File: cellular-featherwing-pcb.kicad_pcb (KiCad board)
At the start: 2 copper layers, 27 x 54 mm, 9 parts, among them J1 SIM8060-6-0-14-00-A, J2 TSM-116-01-L-SV, J3 TSM-112-01-L-SV, U1 BG96, U2 TPS63020DSJR, U3 TXB0108DQSR, U4 MAX8868EUK30+, U5 SN74AHC1G09DCKR

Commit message: Routing progress
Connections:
- U3 pad 12: unconnected-(U3-Pad12) -> GSM_RI
- U5 pad 1: unconnected-(U5-Pad1) -> GSM_RI

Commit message: Add ufl connector
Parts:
- added J4: U.FL-R-SMT(10), U_fl_conn:HRS_U.FL-R-SMT(10), F.Cu at (175.3, 116.8)
- added J5: U.FL-R-SMT(10), U_fl_conn:HRS_U.FL-R-SMT(10), F.Cu at (170.0, 116.8)
- renumbered U5 to DD1
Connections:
- DD1 pad 2: unconnected-(U5-Pad2) -> GSM_RI
- DD1 pad 3: unconnected-(U5-Pad3) -> GND
- DD1 pad 4: unconnected-(U5-Pad4) -> Q_INT
- DD1 pad 5: unconnected-(U5-Pad5) -> 3V3

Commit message: schematic updates
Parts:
- moved J3 1.46 mm to (158.9, 93.0)
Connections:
- net Net-(U1-Pad32) renamed VBAT_BB
- net Net-(U1-Pad52) renamed VBAT_RF
- J2 pad 02: unconnected-(J2-Pad02) -> VDD
- J2 pad 04: unconnected-(J2-Pad04) -> GND
- J2 pad 05: unconnected-(J2-Pad05) -> GMS_STATUS_EXT
- J2 pad 09: unconnected-(J2-Pad09) -> Q_INT_EXT
- J2 pad 10: unconnected-(J2-Pad10) -> GSM_DCD_EXT
- J2 pad 14: unconnected-(J2-Pad14) -> GSM_TXD_ESP32
- J2 pad 15: unconnected-(J2-Pad15) -> GSM_RXD_ESP32
- J3 pad 01: unconnected-(J3-Pad01) -> VBAT
- J3 pad 03: unconnected-(J3-Pad03) -> 5V
- J3 pad 04: unconnected-(J3-Pad04) -> ENABLE
- J3 pad 05: unconnected-(J3-Pad05) -> GSM_RI_EXT
- J3 pad 06: unconnected-(J3-Pad06) -> GSM_TXD_ESP_RTS
- J3 pad 07: unconnected-(J3-Pad07) -> GSM_RXD_ESP_CTS
- J3 pad 09: unconnected-(J3-Pad09) -> MODEM_ON
- J3 pad 10: unconnected-(J3-Pad10) -> GSM_DTR_EXT
- J3 pad 11: unconnected-(J3-Pad11) -> I2C_SCL
- J3 pad 12: unconnected-(J3-Pad12) -> I2C_SDA
- U1 pad 10: unconnected-(U1-Pad10) -> USB_DN_GSM
- U1 pad 15: unconnected-(U1-Pad15) -> ON_PIN
- U1 pad 20: unconnected-(U1-Pad20) -> GSM_STATUS_INT
- U1 pad 21: unconnected-(U1-Pad21) -> GSM_NET
- U1 pad 22: unconnected-(U1-Pad22) -> DBG_RXD
- U1 pad 23: unconnected-(U1-Pad23) -> DBG_TXD
- U1 pad 27: unconnected-(U1-Pad27) -> GPS_TXD
- U1 pad 28: unconnected-(U1-Pad28) -> GPS_RXD
- U1 pad 29: unconnected-(U1-Pad29) -> VDD_EXT
- U1 pad 30: unconnected-(U1-Pad30) -> DTR
- U1 pad 34: unconnected-(U1-Pad34) -> RXD
- U1 pad 35: unconnected-(U1-Pad35) -> TXD
- U1 pad 36: unconnected-(U1-Pad36) -> CTS
- U1 pad 37: unconnected-(U1-Pad37) -> RTS
- U1 pad 38: unconnected-(U1-Pad38) -> DCD
- U1 pad 39: unconnected-(U1-Pad39) -> RI
- U1 pad 42: unconnected-(U1-Pad42) -> GND
- U1 pad 43: unconnected-(U1-Pad43) -> SIM_VDD
- U1 pad 44: unconnected-(U1-Pad44) -> SIM_RST
- U1 pad 45: unconnected-(U1-Pad45) -> SIM_DATA
- U1 pad 46: unconnected-(U1-Pad46) -> SIM_CLK
- U1 pad 47: unconnected-(U1-Pad47) -> GND
- U1 pad 49: unconnected-(U1-Pad49) -> GPS_ANT
- U1 pad 60: unconnected-(U1-Pad60) -> GSM_ANT
- U1 pad 75: unconnected-(U1-Pad75) -> USB_BOOT
- U1 pad 8: unconnected-(U1-Pad8) -> USB_VBUS_GSM
- U1 pad 9: unconnected-(U1-Pad9) -> USB_DP_GSM
- U3 pad 1: unconnected-(U3-Pad1) -> RXD
- U3 pad 10: unconnected-(U3-Pad10) -> GSM_STATUS_INT
- U3 pad 11: unconnected-(U3-Pad11) -> GSM_STATUS
- U3 pad 13: unconnected-(U3-Pad13) -> GSM_DCD
- U3 pad 14: unconnected-(U3-Pad14) -> GSM_DTR
- U3 pad 15: unconnected-(U3-Pad15) -> GND
- U3 pad 16: unconnected-(U3-Pad16) -> 3V3
- U3 pad 17: unconnected-(U3-Pad17) -> GSM_CTS
- U3 pad 18: unconnected-(U3-Pad18) -> GSM_RTS
- U3 pad 19: unconnected-(U3-Pad19) -> GSM_TXD
- U3 pad 2: unconnected-(U3-Pad2) -> TXD
- U3 pad 20: unconnected-(U3-Pad20) -> GSM_RXD
- U3 pad 3: unconnected-(U3-Pad3) -> RTS_GPS_RXD
- U3 pad 4: unconnected-(U3-Pad4) -> CTS_GPS_TXD
- U3 pad 5: unconnected-(U3-Pad5) -> VDD_EXT
- U3 pad 6: unconnected-(U3-Pad6) -> VDD_EXT
- U3 pad 7: unconnected-(U3-Pad7) -> DTR
- U3 pad 8: unconnected-(U3-Pad8) -> DCD
- U3 pad 9: unconnected-(U3-Pad9) -> RI

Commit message: More progress
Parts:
- added VT3: DTC043TEBTL, ul_DTC043TEBTL:DTC043TEBTL, F.Cu at (146.6, 132.7)
- added VT4: DTC043TEBTL, ul_DTC043TEBTL:DTC043TEBTL, F.Cu at (156.5, 132.7)

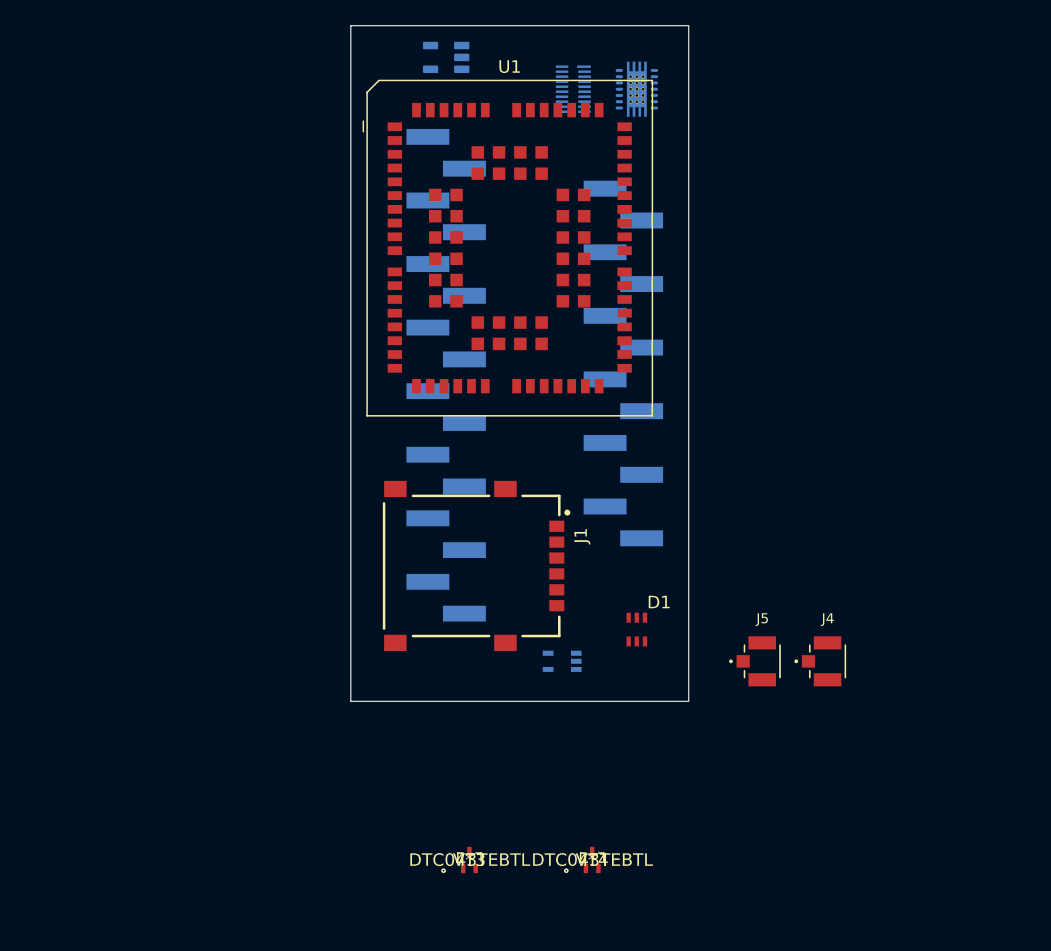
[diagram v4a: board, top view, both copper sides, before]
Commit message: Wired network LED in schematic
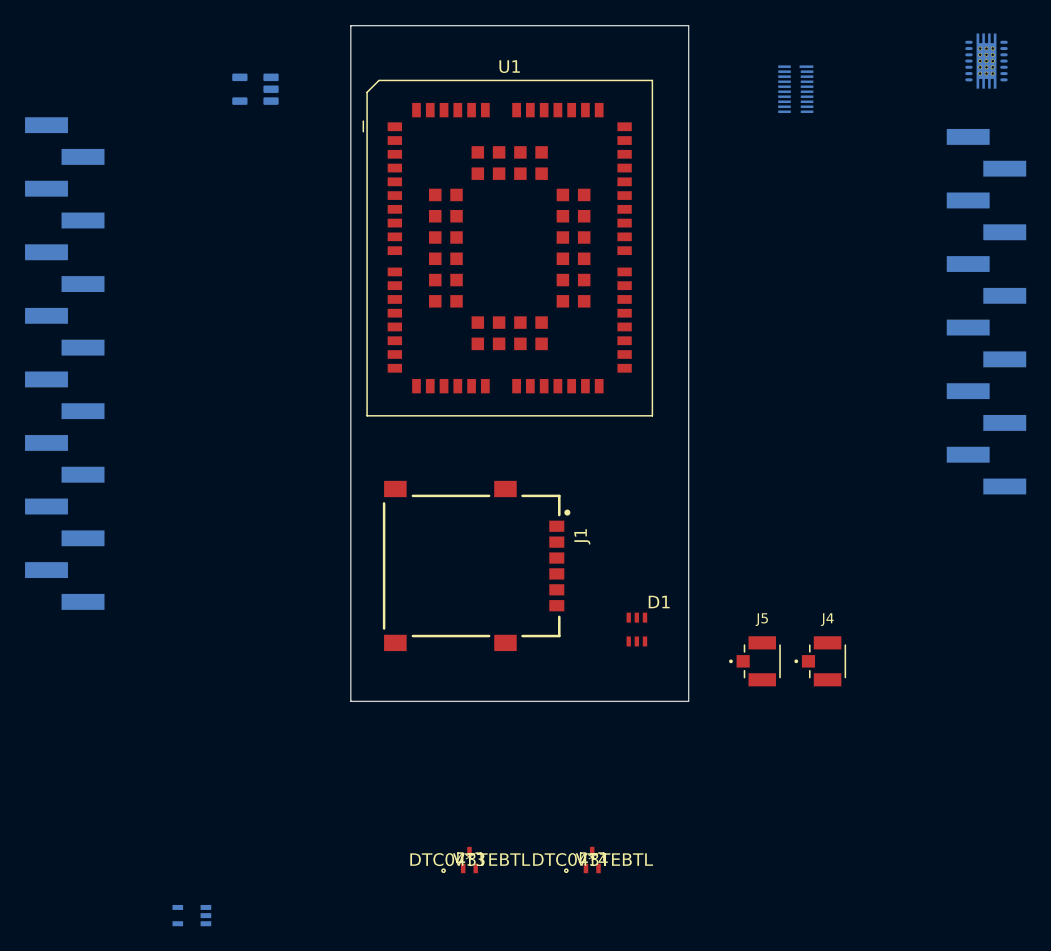
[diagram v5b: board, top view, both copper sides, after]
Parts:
- moved DD1 35.9 mm to (124.5, 137.2)
- moved J2 30.5 mm to (114.3, 93.0)
- moved J3 29.3 mm to (188.0, 88.9)
- moved U2 28.0 mm to (188.0, 68.9)
- moved U3 17.8 mm to (172.7, 71.1)
- moved U4 15.5 mm to (129.5, 71.1)
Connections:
- D1 pad 2: unconnected-(D1-Pad2) -> GND
- D1 pad 3: unconnected-(D1-Pad3) -> SIM_VDD
- D1 pad 4: unconnected-(D1-Pad4) -> Net-(J1-PadC2)
- D1 pad 6: unconnected-(D1-Pad6) -> Net-(J1-PadC3)
- J1 pad C1: unconnected-(J1-PadC1) -> SIM_VDD
- J1 pad C2: unconnected-(J1-PadC2) -> Net-(J1-PadC2)
- J1 pad C3: unconnected-(J1-PadC3) -> Net-(J1-PadC3)
- J1 pad C5: unconnected-(J1-PadC5) -> GND
- J1 pad C7: unconnected-(J1-PadC7) -> Net-(J1-PadC7)
- J1 pad S1: Net-(J1-PadS1) -> GND
- J1 pad S2: Net-(J1-PadS1) -> GND
- J1 pad S3: Net-(J1-PadS1) -> GND
- J1 pad S4: Net-(J1-PadS1) -> GND

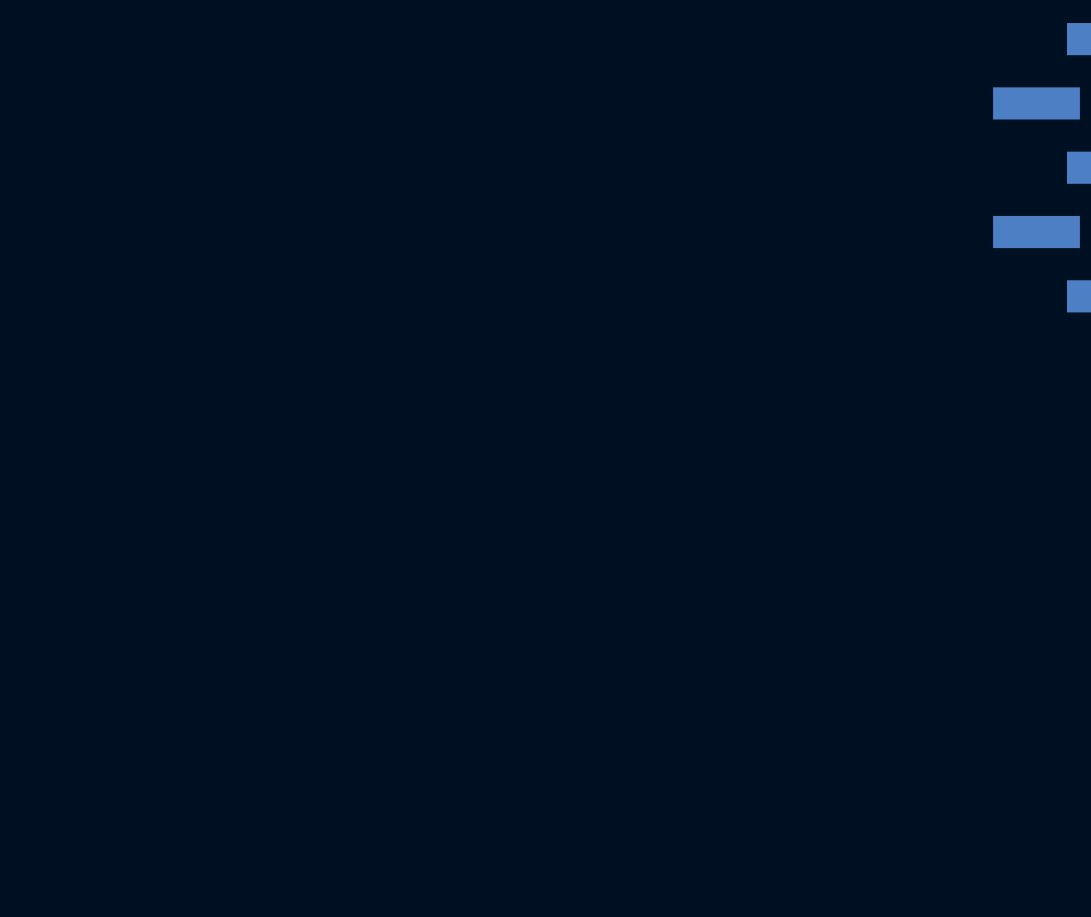
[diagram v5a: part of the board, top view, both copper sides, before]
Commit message: Wired all the jumpers
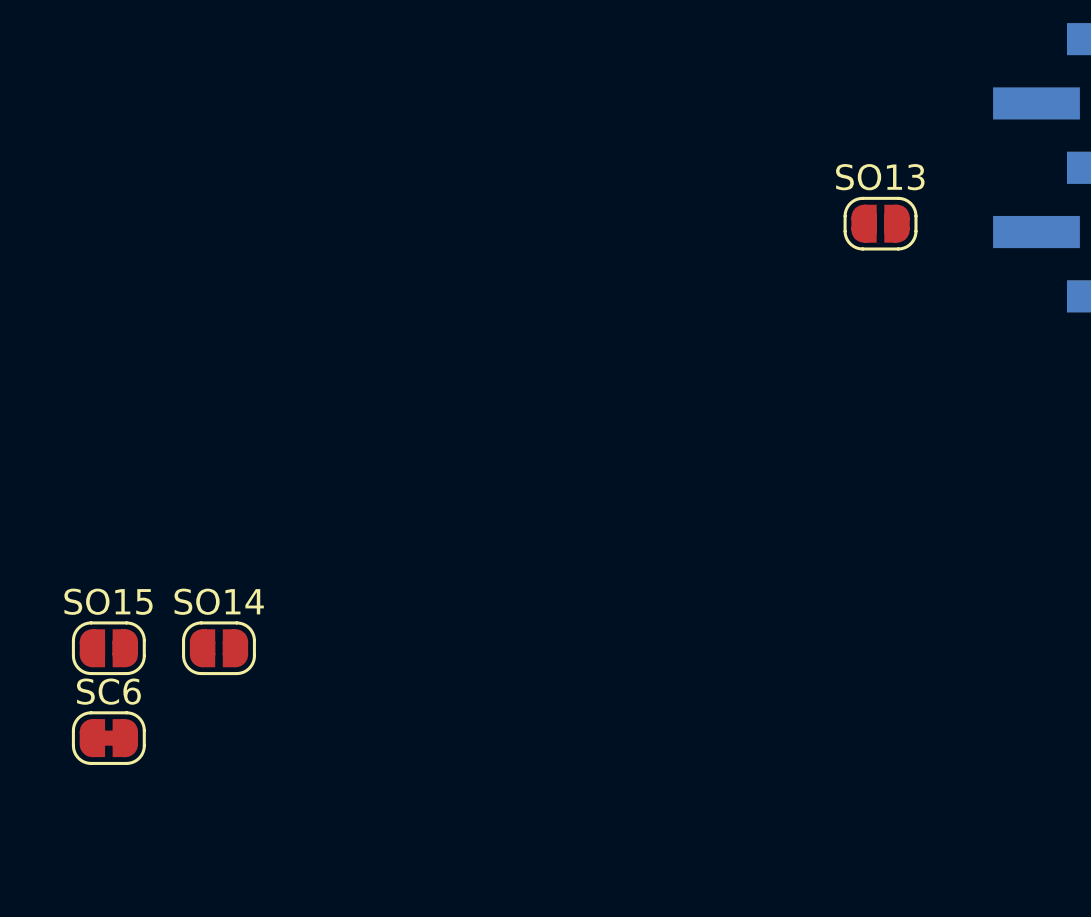
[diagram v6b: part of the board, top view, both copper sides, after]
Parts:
- added SC6: SolderJumper_2_Bridged, Jumper:SolderJumper-2_P1.3mm_Bridged_RoundedPad1.0x1.5mm, F.Cu at (76.2, 129.5)
- added SO13: SolderJumper_2_Open, Jumper:SolderJumper-2_P1.3mm_Open_RoundedPad1.0x1.5mm, F.Cu at (106.7, 109.2)
- added SO14: SolderJumper_2_Open, Jumper:SolderJumper-2_P1.3mm_Open_RoundedPad1.0x1.5mm, F.Cu at (80.5, 126.0)
- added SO15: SolderJumper_2_Open, Jumper:SolderJumper-2_P1.3mm_Open_RoundedPad1.0x1.5mm, F.Cu at (76.2, 126.0)
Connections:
- U4 pad 2: unconnected-(U4-Pad2) -> GND

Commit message: schematic complete
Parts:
- added C1: 22uF, Capacitor_SMD:C_0603_1608Metric, F.Cu at (177.8, 134.6)
- added C2: 22uF, Capacitor_SMD:C_0603_1608Metric, F.Cu at (177.8, 132.1)
- added C30: 4.7uF, Capacitor_SMD:C_0402_1005Metric, F.Cu at (73.7, 86.4)
- added C31: 4.7uF, Capacitor_SMD:C_0402_1005Metric, F.Cu at (68.1, 95.5)
- added C33: 4.7uF, Capacitor_SMD:C_0402_1005Metric, F.Cu at (71.0, 95.7)
- added C6: 22uF, Capacitor_SMD:C_0603_1608Metric, F.Cu at (181.8, 134.6)
- added C7: 22uF, Capacitor_SMD:C_0603_1608Metric, F.Cu at (177.8, 137.1)
- added C8: 22uF, Capacitor_SMD:C_0603_1608Metric, F.Cu at (181.8, 132.1)
- added L1: 1 uH, Inductor_SMD:L_Coilcraft_XxL4020, F.Cu at (87.5, 50.8)
- added SC1: SolderJumper_2_Bridged, Jumper:SolderJumper-2_P1.3mm_Bridged_RoundedPad1.0x1.5mm, F.Cu at (87.4, 90.9)
- added SC2: SolderJumper_2_Bridged, Jumper:SolderJumper-2_P1.3mm_Bridged_RoundedPad1.0x1.5mm, F.Cu at (81.9, 94.5)
- added SC3: SolderJumper_2_Bridged, Jumper:SolderJumper-2_P1.3mm_Bridged_RoundedPad1.0x1.5mm, F.Cu at (77.5, 94.5)
- added SC4: SolderJumper_2_Bridged, Jumper:SolderJumper-2_P1.3mm_Bridged_RoundedPad1.0x1.5mm, F.Cu at (88.6, 83.8)
- added SO1: SolderJumper_2_Open, Jumper:SolderJumper-2_P1.3mm_Open_RoundedPad1.0x1.5mm, F.Cu at (83.0, 87.3)
- added SO10: SolderJumper_2_Open, Jumper:SolderJumper-2_P1.3mm_Open_RoundedPad1.0x1.5mm, F.Cu at (87.4, 87.3)
- added SO11: SolderJumper_2_Open, Jumper:SolderJumper-2_P1.3mm_Open_RoundedPad1.0x1.5mm, F.Cu at (78.7, 87.3)
- added SO12: SolderJumper_2_Open, Jumper:SolderJumper-2_P1.3mm_Open_RoundedPad1.0x1.5mm, F.Cu at (73.2, 92.9)
- added SO2: SolderJumper_2_Open, Jumper:SolderJumper-2_P1.3mm_Open_RoundedPad1.0x1.5mm, F.Cu at (78.7, 90.9)
- added SO4: SolderJumper_2_Open, Jumper:SolderJumper-2_P1.3mm_Open_RoundedPad1.0x1.5mm, F.Cu at (79.9, 83.8)
- added SO5: SolderJumper_2_Open, Jumper:SolderJumper-2_P1.3mm_Open_RoundedPad1.0x1.5mm, F.Cu at (83.0, 90.9)
- added SO6: SolderJumper_2_Open, Jumper:SolderJumper-2_P1.3mm_Open_RoundedPad1.0x1.5mm, F.Cu at (84.2, 83.8)
- added SO7: SolderJumper_2_Open, Jumper:SolderJumper-2_P1.3mm_Open_RoundedPad1.0x1.5mm, F.Cu at (74.3, 89.4)
- added SO8: SolderJumper_2_Open, Jumper:SolderJumper-2_P1.3mm_Open_RoundedPad1.0x1.5mm, F.Cu at (92.9, 83.8)
- added SO9: SolderJumper_2_Open, Jumper:SolderJumper-2_P1.3mm_Open_RoundedPad1.0x1.5mm, F.Cu at (68.8, 92.7)
- added VD5: SS2030FL_R1_00001, Diode_SMD:D_SOD-123F, F.Cu at (75.0, 83.7)
- added VD6: SS2030FL_R1_00001, Diode_SMD:D_SOD-123F, F.Cu at (58.4, 71.1)
- U2: value TPS63020DSJR -> TPS63020QDSJTQ1
- U4: value MAX8868EUK30+ -> MAX8868EUK30+T
- moved U2 108.2 mm to (81.3, 50.8)
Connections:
- net GSM_STATUS_EXT renamed GSM_INT_EXT
- J4 pad 2: Net-(J4-Pad2) -> GND
- J4 pad 3: Net-(J4-Pad2) -> GND
- U2 pad 1: unconnected-(U2-Pad1) -> Net-(U2-Pad1)
- U2 pad 10: unconnected-(U2-Pad10) -> VIN
- U2 pad 11: unconnected-(U2-Pad11) -> VIN
- U2 pad 12: unconnected-(U2-Pad12) -> ENABLE
- U2 pad 13: unconnected-(U2-Pad13) -> VIN
- U2 pad 15: unconnected-(U2-Pad15) -> GND
- U2 pad 2: unconnected-(U2-Pad2) -> GND
- U2 pad 3: unconnected-(U2-Pad3) -> Net-(U2-Pad3)
- U2 pad 4: unconnected-(U2-Pad4) -> Net-(C7-Pad1)
- U2 pad 5: unconnected-(U2-Pad5) -> Net-(C7-Pad1)
- U2 pad 6: unconnected-(U2-Pad6) -> Net-(L1-Pad1)
- U2 pad 7: unconnected-(U2-Pad7) -> Net-(L1-Pad1)
- U2 pad 8: unconnected-(U2-Pad8) -> Net-(U2-Pad8)
- U2 pad 9: unconnected-(U2-Pad9) -> Net-(U2-Pad8)
- U4 pad 1: unconnected-(U4-Pad1) -> VMODEM
- U4 pad 3: unconnected-(U4-Pad3) -> VMODEM
- U4 pad 4: unconnected-(U4-Pad4) -> 3V3
- U4 pad 5: unconnected-(U4-Pad5) -> Net-(U4-Pad5)

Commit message: All footprints assigned
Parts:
- added C10: DNP, Capacitor_SMD:C_0402_1005Metric, F.Cu at (98.8, 142.2)
- added C13: DNP, Capacitor_SMD:C_0402_1005Metric, F.Cu at (92.0, 149.3)
- added C14: DNP, Capacitor_SMD:C_0402_1005Metric, F.Cu at (95.7, 148.3)
- added C15: 0.1uF, Capacitor_SMD:C_0402_1005Metric, F.Cu at (98.8, 140.2)
- added C20: 100nF, Capacitor_SMD:C_0402_1005Metric, F.Cu at (98.8, 144.1)
- added C21: 100nF, Capacitor_SMD:C_0402_1005Metric, F.Cu at (91.8, 152.4)
- added C22: 33pF, Capacitor_SMD:C_0402_1005Metric, F.Cu at (80.9, 155.5)
- added C23: 33pF, Capacitor_SMD:C_0402_1005Metric, F.Cu at (95.7, 146.3)
- added C24: 10pF, Capacitor_SMD:C_0402_1005Metric, F.Cu at (87.6, 154.4)
- added C25: 10pF, Capacitor_SMD:C_0402_1005Metric, F.Cu at (78.0, 155.5)
- added C26: C_Polarized_US, Capacitor_Tantalum_SMD:CP_EIA-3528-12_Kemet-T, F.Cu at (75.6, 145.7)
- added C28: C_Polarized_US, Capacitor_Tantalum_SMD:CP_EIA-3528-12_Kemet-T, F.Cu at (75.6, 141.4)
- added C9: DNP, Capacitor_SMD:C_0402_1005Metric, F.Cu at (88.9, 152.4)
- added FB1: FerriteBead, Resistor_SMD:R_0805_2012Metric, F.Cu at (74.8, 149.4)
- added FB2: FerriteBead, Resistor_SMD:R_0805_2012Metric, F.Cu at (74.8, 152.3)
- added FB3: FerriteBead, Resistor_SMD:R_0805_2012Metric, F.Cu at (86.0, 140.7)
- added FB4: FerriteBead, Resistor_SMD:R_0805_2012Metric, F.Cu at (80.8, 146.2)
- added J5: U.FL-R-SMT, U_fl_conn:HRS_U.FL-R-SMT(10), F.Cu at (81.7, 142.0)
- added R6: 0, Capacitor_SMD:C_0402_1005Metric, F.Cu at (101.7, 140.2)
- added R7: 10, Capacitor_SMD:C_0603_1608Metric, F.Cu at (74.6, 155.1)
- added SO17: SolderJumper_2_Open, Jumper:SolderJumper-2_P1.3mm_Open_RoundedPad1.0x1.5mm, F.Cu at (86.0, 143.9)
- added SO18: SolderJumper_2_Open, Jumper:SolderJumper-2_P1.3mm_Open_RoundedPad1.0x1.5mm, F.Cu at (79.2, 149.7)
- added TP1: TestPoint, TestPoint:TestPoint_Pad_D1.0mm, F.Cu at (81.6, 153.0)
- added TP10: TestPoint, TestPoint:TestPoint_Pad_D1.0mm, F.Cu at (92.8, 140.7)
- added TP11: TestPoint, TestPoint:TestPoint_Pad_D1.0mm, F.Cu at (89.7, 143.8)
- added TP12: TestPoint, TestPoint:TestPoint_Pad_D1.0mm, F.Cu at (89.0, 149.9)
- added TP13: TestPoint, TestPoint:TestPoint_Pad_D1.0mm, F.Cu at (95.8, 140.7)
- added TP14: TestPoint, TestPoint:TestPoint_Pad_D1.0mm, F.Cu at (85.9, 147.2)
- added TP15: TestPoint, TestPoint:TestPoint_Pad_D1.0mm, F.Cu at (78.5, 153.0)
- added TP2: TestPoint, TestPoint:TestPoint_Pad_D1.0mm, F.Cu at (84.6, 153.3)
- added TP3: TestPoint, TestPoint:TestPoint_Pad_D1.0mm, F.Cu at (85.9, 150.3)
- added TP4: TestPoint, TestPoint:TestPoint_Pad_D1.0mm, F.Cu at (82.9, 149.2)
- added TP5: TestPoint, TestPoint:TestPoint_Pad_D1.0mm, F.Cu at (89.8, 140.7)
- added TP6: TestPoint, TestPoint:TestPoint_Pad_D1.0mm, F.Cu at (92.7, 146.8)
- added TP7: TestPoint, TestPoint:TestPoint_Pad_D1.0mm, F.Cu at (95.8, 143.8)
- added TP8: TestPoint, TestPoint:TestPoint_Pad_D1.0mm, F.Cu at (92.7, 143.8)
- added TP9: TestPoint, TestPoint:TestPoint_Pad_D1.0mm, F.Cu at (89.7, 146.8)
- J4: value U.FL-R-SMT(10) -> U.FL-R-SMT
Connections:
- C1 pad 1: VIN -> Net-(FB1-Pad2)
- C2 pad 1: VIN -> Net-(FB1-Pad2)
- J4 pad 1: unconnected-(J4-Pad1) -> Net-(J4-Pad1)
- U2 pad 10: VIN -> Net-(FB1-Pad2)
- U2 pad 11: VIN -> Net-(FB1-Pad2)
- U2 pad 13: VIN -> Net-(FB1-Pad2)
